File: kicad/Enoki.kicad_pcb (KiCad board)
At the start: 2 copper layers, 40 x 23 mm, 18 parts, among them J1 Conn_01x08_Male, J2 Conn_01x02_Pin, J3 Conn_01x02_Pin

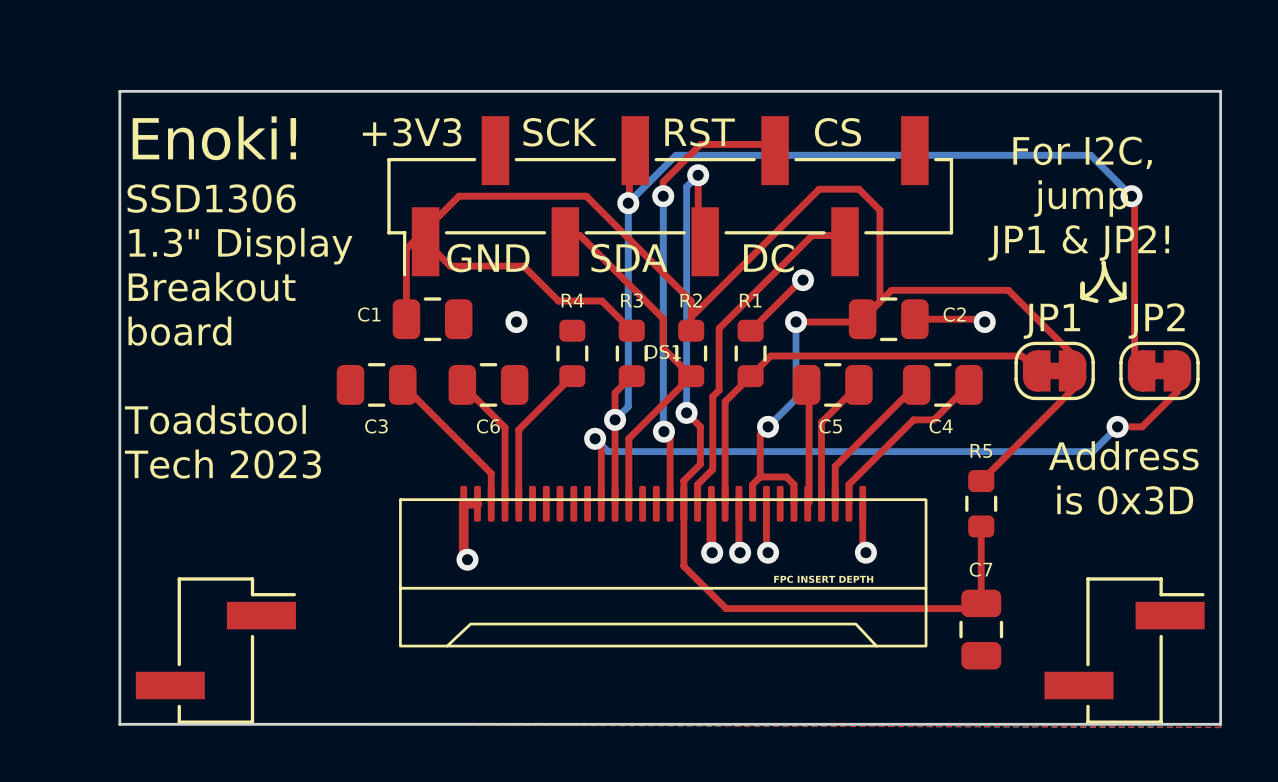
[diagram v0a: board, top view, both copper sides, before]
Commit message: move board to place header pins on grid
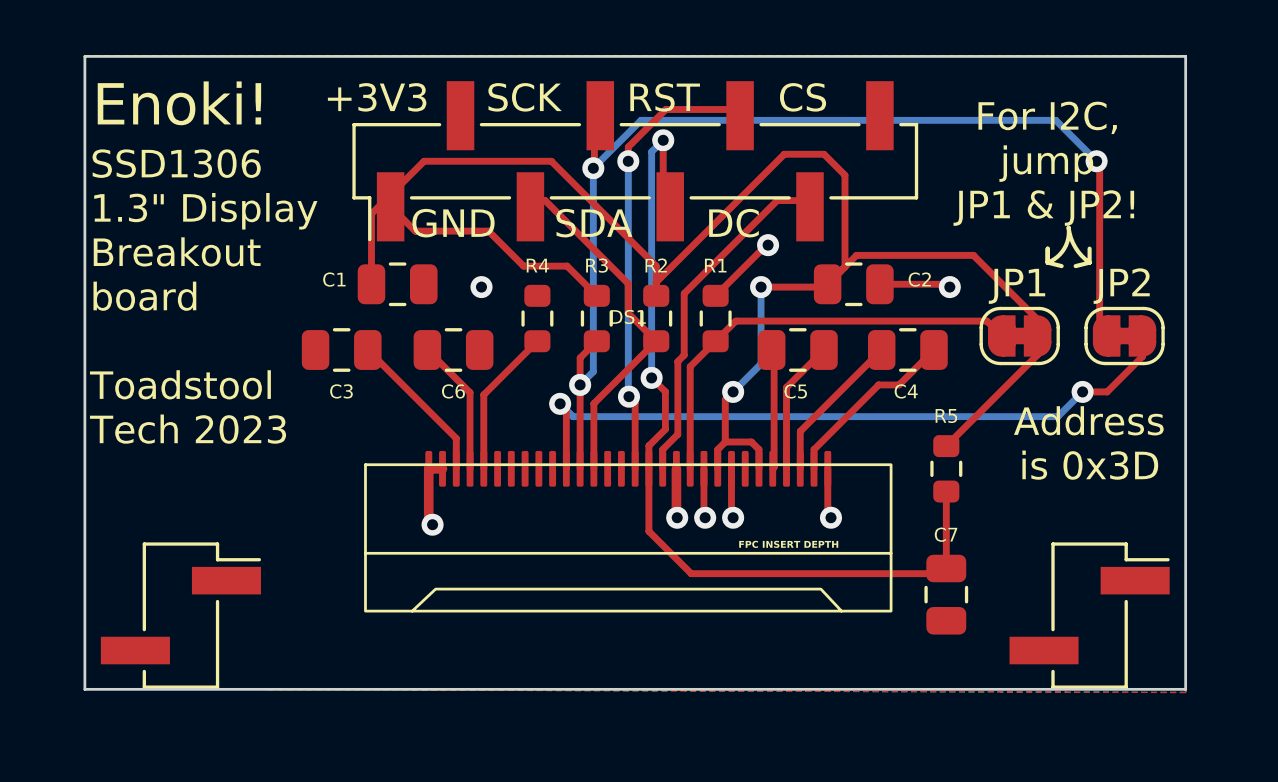
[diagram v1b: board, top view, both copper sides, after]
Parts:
- moved C2 1.80 mm to (27.0, 7.01)
- moved C5 1.80 mm to (25.0, 9.40)
- moved JP2 1.80 mm to (36.8, 8.89)
- moved R5 1.80 mm to (30.4, 13.7)
- moved C1 1.80 mm to (10.4, 7.01)
- moved J1 1.80 mm to (19.1, 2.54)
- moved J2 1.80 mm to (2.54, 19.1)
- moved C3 1.80 mm to (8.38, 9.40)
- moved C4 1.80 mm to (29.0, 9.40)
- moved C6 1.80 mm to (12.4, 9.40)
- moved C7 1.80 mm to (30.4, 18.3)
- moved DS1 1.80 mm to (18.8, 16.8)
- moved R1 1.80 mm to (22.0, 8.26)
- moved R2 1.80 mm to (19.8, 8.26)
- moved R3 1.80 mm to (17.7, 8.26)
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
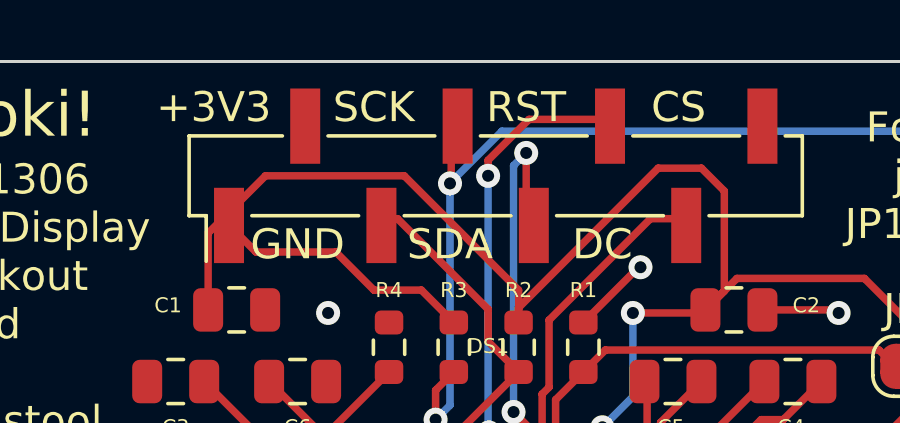
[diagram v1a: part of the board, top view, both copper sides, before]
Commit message: use RES and SCL as per SSD1306 datasheet
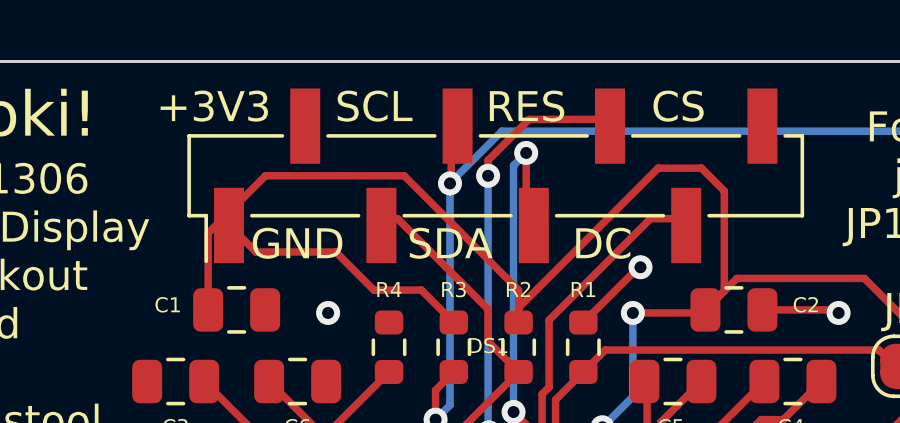
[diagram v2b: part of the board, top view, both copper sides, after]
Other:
- board text added: "RES"
- board text added: "SCL"
- board text removed: "RST"
- board text removed: "SCK"

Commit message: update year to 2024
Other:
- board text added: "SSD1306 1.3{dblquote} Display Breakout board Toadstool Tech 2024"
- board text removed: "SSD1306 1.3{dblquote} Display Breakout board Toadstool Tech 2023"
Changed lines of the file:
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@@
     (effects (font (size 1 1) (thickness 0.15)))
   )
-  (gr_text "SSD1306\n1.3{dblquote} Display\nBreakout \nboard\n\nToadstool \nTech 2023" (at -0.762 7.493) (layer "F.SilkS")
+  (gr_text "SSD1306\n1.3{dblquote} Display\nBreakout \nboard\n\nToadstool \nTech 2024" (at -0.762 7.493) (layer "F.SilkS")
     (effects (font (size 1 1) (thickness 0.15)) (justify left))
   )
